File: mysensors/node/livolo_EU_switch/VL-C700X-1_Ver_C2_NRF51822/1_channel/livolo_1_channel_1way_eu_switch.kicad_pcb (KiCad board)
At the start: 2 copper layers, 43 x 43.4 mm, 40 parts, among them J1 SWD, P1 Sense Pad 1, P2 Sense Pad 2, P4 Power Board, U1 MIC5205-3.0*, U2 MCP16301, U3 TTP223, U4 TTP223, U5 PTR5518

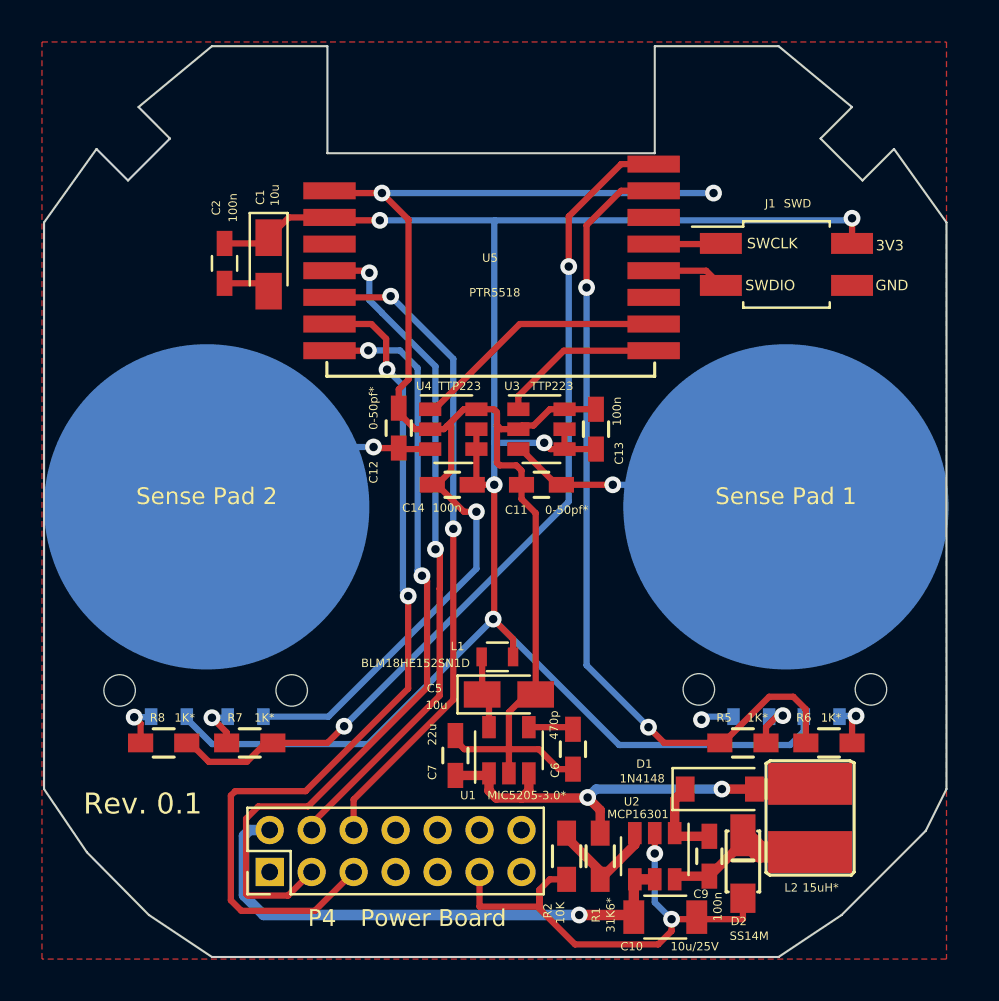
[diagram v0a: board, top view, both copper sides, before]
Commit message: [mysensors] added livolo nrf51822 1 channel variant
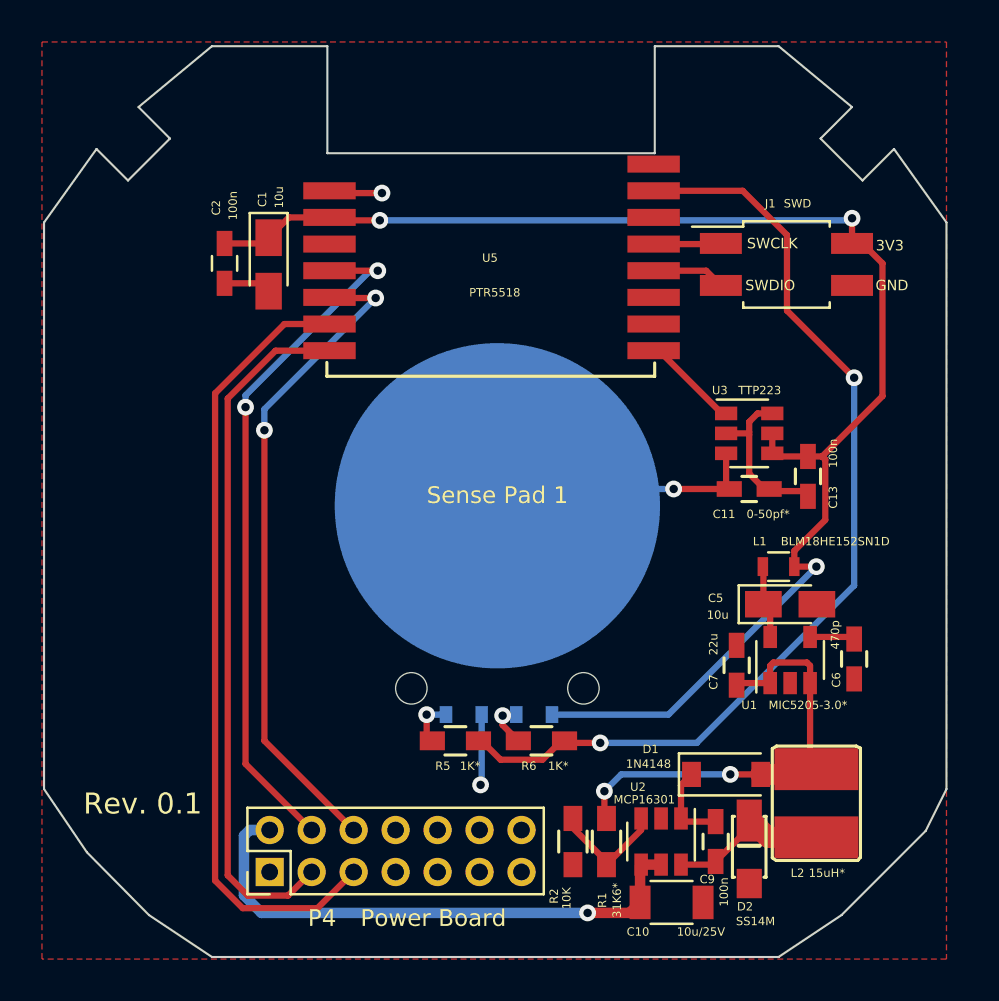
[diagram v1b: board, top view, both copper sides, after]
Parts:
- removed C12: 0-50pf*, Capacitors_SMD:C_0603_HandSoldering
- removed C14: 100n, Capacitors_SMD:C_0603_HandSoldering
- removed D3: Blue, Diodes_SMD:D_0603
- removed D4: Red, Diodes_SMD:D_0603
- removed P2: Sense Pad 2, myfootprints:touch_pad_16mm
- removed R7, R8: 1K*, Resistors_SMD:R_0603_HandSoldering
- removed the REF** at (142.3, 92.0)
- removed the REF** at (152.1, 100.8)
- removed the REF** at (160.3, 100.8)
- removed U4: TTP223, TO_SOT_Packages_SMD:SOT-23-6
- added REF**: Livolo_EU_SW_2Ways_Frame_VL-C702X-2_Ver_C1, myfootprints:Livolo_EU_SW_1_Channel_1Way_Frame_VL-C702X-2_Ver_C1, B.Cu at (142.3, 92.0)
- moved C6 14.1 mm to (159.5, 99.4)
- moved C7 14.1 mm to (153.9, 99.7)
- moved L1 14.1 mm to (155.9, 95.0)
- moved C5 14.1 mm to (156.4, 96.8)
- moved U1 14.1 mm to (156.4, 99.5)
- moved REF** 13.9 mm to (146.6, 100.8)
- moved REF** 13.9 mm to (138.4, 100.8)
- moved P1 13.8 mm to (142.5, 92.1)
- moved R6 13.7 mm to (144.6, 103.3), turned to 0 degrees
- moved D5 13.7 mm to (144.2, 102.0), turned to 0 degrees
- moved D6 13.7 mm to (140.9, 102.0), turned to 180 degrees
- moved R5 13.7 mm to (140.5, 103.3), turned to 0 degrees
- moved C13 10.3 mm to (157.3, 90.7), turned to 270 degrees
- moved C11 9.90 mm to (154.5, 91.3), turned to 0 degrees
- moved U3 9.90 mm to (154.5, 88.7)
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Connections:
- U5 pad 2: /TS2 -> (no net)
- U5 pad 8: /S2_LEDs -> (no net)
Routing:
- net GND: track 115.6 -> 16.2 mm, vias 6 -> 2
- net /S2_LEDs: track 42.4 -> 0.00 mm, vias 2 -> 0
- net +3V3: track 98.8 -> 70.3 mm, vias 5 -> 3
- net /TS2: track 12.3 -> 0.00 mm
- net Net-(C12-Pad1): track 11.9 -> 0.00 mm, vias 1 -> 0
- net /S1_LEDs: track 39.8 -> 47.0 mm
- net /Relay2_Reset: track 38.4 -> 33.4 mm, vias 2 -> 0
- net /Relay2_Set: track 42.5 -> 37.9 mm, vias 2 -> 0
- net /TS1: track 7.97 -> 4.69 mm
- net Net-(D3-Pad2): track 2.26 -> 0.00 mm, vias 1 -> 0
- net Net-(D4-Pad1): track 2.17 -> 0.00 mm, vias 1 -> 0
- net /Relay1_Set: track 32.6 -> 33.4 mm
- net Net-(C11-Pad1): track 13.9 -> 13.1 mm
- net /12Vcc: track 25.9 -> 26.5 mm

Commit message: new stuff
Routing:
- net GND: track 16.2 -> 13.9 mm, vias 2 -> 1
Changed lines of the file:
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@@
-(kicad_pcb (version 20170123) (host pcbnew no-vcs-found-d37a337~58~ubuntu16.04.1)
+(kicad_pcb (version 20170123) (host pcbnew no-vcs-found-2237de0~58~ubuntu16.04.1)
   (general
-    (links 56)
-    (no_connects 0)
-    (area 120.568279 70 164.267941 113.934921)
     (thickness 1.6)
     (drawings 37)
-    (tracks 169)
+    (tracks 167)
     (zones 0)
     (modules 30)
@@
   (segment (start 129.5 81.5) (end 131.225 81.5) (width 0.3) (layer F.Cu) (net 2) (status 30))
   (segment (start 131.225 81.5) (end 131.6 81.875) (width 0.3) (layer F.Cu) (net 2) (status 30))
-  (segment (start 137 77.2) (end 134.61 77.2) (width 0.3) (layer F.Cu) (net 2) (status 20))
   (segment (start 134.61 77.2) (end 134.5 77.09) (width 0.3) (layer F.Cu) (net 2) (status 30))
-  (via (at 137 77.2) (size 0.8) (drill 0.4) (layers F.Cu B.Cu) (net 2))
   (segment (start 157.4 98.35) (end 159.4 98.35) (width 0.3) (layer F.Cu) (net 3) (status 30))
   (segment (start 159.4 98.35) (end 159.5 98.45) (width 0.3) (layer F.Cu) (net 3) (status 30))

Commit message: mysensors nrf5 livolo node one channel - final touches
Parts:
- removed C11: 0-50pf*, Capacitors_SMD:C_0603_HandSoldering
- removed C13: 100n, Capacitors_SMD:C_0603_HandSoldering
- removed C5: 10u, Capacitors_Tantalum_SMD:CP_Tantalum_Case-R_EIA-2012-12_Wave
- removed C6: 470p, Capacitors_SMD:C_0603_HandSoldering
- removed P1: Sense Pad 1, myfootprints:touch_pad_16mm
- removed REF***: OSHW-Logo2_7.3x6mm_SilkScreen, Symbols:OSHW-Logo2_7.3x6mm_SilkScreen
- added C3: 100n, Capacitors_SMD:C_0603_HandSoldering, F.Cu at (155.4, 88.8)
- added C4: 1u, Capacitors_SMD:C_0603_HandSoldering, F.Cu at (159.8, 95.4)
- added G***: LOGO, w_logo:Logo_silk_OSHW_6x6mm, B.Cu at (142.4, 80.0)
- added R3: 0, Resistors_SMD:R_0603, F.Cu at (152.8, 94.0)
- added R4: 4K7, Resistors_SMD:R_0603, F.Cu at (152.8, 92.2)
- added R7: 10K, Resistors_SMD:R_0603_HandSoldering, F.Cu at (158.2, 89.8)
- added R8: 4K7, Resistors_SMD:R_0603_HandSoldering, F.Cu at (162.4, 92.6)
- L2: value 15uH* -> 15uH
- R1: value 31K6* -> 31K6
- U1: value MIC5205-3.0* -> Touch; footprint TO_SOT_Packages_SMD:SOT-23-5 -> myfootprints:livolo_ts_guard
- U3: value TTP223 -> MTCH102; footprint TO_SOT_Packages_SMD:SOT-23-6 -> Housings_SSOP:MSOP-8_3x3mm_Pitch0.65mm
- moved U1 15.7 mm to (142.6, 91.9), turned to 45 degrees
- moved L1 5.95 mm to (153.4, 100.4)
- moved U3 5.15 mm to (157.8, 92.6)
- moved C7 3.00 mm to (155.2, 102.4), turned to 0 degrees
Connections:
- L1 pad 1: +3V3 -> Net-(C7-Pad1)
- L1 pad 2: Net-(C5-Pad1) -> +3V3
- P4 pad 1: (no net) -> Net-(P4-Pad1)
- P4 pad 10: (no net) -> Net-(P4-Pad10)
- P4 pad 12: (no net) -> Net-(P4-Pad12)
- P4 pad 13: (no net) -> Net-(P4-Pad13)
- P4 pad 14: (no net) -> Net-(P4-Pad14)
- P4 pad 7: (no net) -> Net-(P4-Pad7)
- P4 pad 8: (no net) -> Net-(P4-Pad8)
- P4 pad 9: (no net) -> Net-(P4-Pad9)
- U1 pad 1: Net-(C7-Pad1) -> Net-(R4-Pad2)
- U1 pad 2: GND -> Net-(R3-Pad2)
- U3 pad 1: /TS1 -> +3V3
- U3 pad 2: GND -> Net-(R4-Pad1)
- U3 pad 4: +3V3 -> /MTPM
- U3 pad 5: +3V3 -> Net-(C4-Pad1)
- U5 pad 11: (no net) -> /S1_LEDs
- U5 pad 2: (no net) -> /MTSA
- U5 pad 3: (no net) -> /MTPM
- U5 pad 7: /S1_LEDs -> Net-(U5-Pad7)
- U5 pad 8: (no net) -> Net-(U5-Pad8)
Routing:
- net GND: track 13.9 -> 73.9 mm, vias 1 -> 5
- net /MTPM: track 0.00 -> 17.4 mm, vias 0 -> 2
- net /MTSA: track 0.00 -> 16.3 mm
- net Net-(R3-Pad2): track 0.00 -> 13.8 mm
- net /TS1: track 4.69 -> 15.9 mm
- net Net-(R3-Pad1): track 13.1 -> 2.56 mm, vias 1 -> 0
- net Net-(R4-Pad2): track 0.00 -> 10.1 mm, vias 0 -> 1
- net Net-(C7-Pad1): track 21.4 -> 16.0 mm
- net Net-(C4-Pad1): track 0.00 -> 5.03 mm
- net +3V3: track 70.3 -> 66.5 mm, vias 3 -> 4
- net Net-(C5-Pad1): track 3.49 -> 0.00 mm
- net /S1_LEDs: track 47.0 -> 44.6 mm
- net Net-(R4-Pad1): track 0.00 -> 2.16 mm
- net Net-(C6-Pad1): track 2.14 -> 0.00 mm
- net /Relay2_Set: track 37.9 -> 40.0 mm
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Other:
- net class Default: clearance 0.3 -> 0.25; trace_width 0.3 -> 0.25
- rule trace_clearance: 0.3 -> 0.25
- board text added: "Rev. 0.2"
- board text removed: "Rev. 0.1"

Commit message: mysensors nrf5 livolo node one channel - final touches
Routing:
- net Net-(D6-Pad2): track 2.78 -> 2.26 mm
